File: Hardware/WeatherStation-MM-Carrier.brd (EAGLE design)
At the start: 67.3 x 58.4 mm, 154 parts, among them J11 microSD, J13 RJ11 - WIND, J15 MICROMOD-2222-C, J2 JTAG, J3 QWIIC_RIGHT_ANGLE, J7 RJ11 - RAIN, U1 BME280, U2 VEML6075, U3 AS3935, U5 AP7361C-33FGE

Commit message: Implementing some changes from design check list
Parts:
- removed U$24: (no value), buzzard_labels (3):STATION5
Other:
- board text added: "ROUTE OUT"
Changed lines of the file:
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@@
 <layer number="25" name="tNames" color="7" fill="1" visible="no" active="yes"/>
 <layer number="26" name="bNames" color="7" fill="1" visible="no" active="yes"/>
-<layer number="27" name="tValues" color="7" fill="1" visible="yes" active="yes"/>
+<layer number="27" name="tValues" color="7" fill="1" visible="no" active="yes"/>
 <layer number="28" name="bValues" color="7" fill="1" visible="no" active="yes"/>
 <layer number="29" name="tStop" color="7" fill="3" visible="no" active="yes"/>
@@
 <rectangle x1="20.32" y1="56.261" x2="25.4" y2="58.039" layer="21"/>
 <rectangle x1="20.32" y1="56.261" x2="25.4" y2="58.039" layer="22" rot="R180"/>
+<text x="36.83" y="40.64" size="0.254" layer="20" font="vector" ratio="15">ROUTE OUT</text>
+<text x="35.56" y="36.83" size="0.254" layer="20" font="vector" ratio="15" rot="R90">ROUTE OUT</text>
+<text x="40.64" y="39.37" size="0.254" layer="20" font="vector" ratio="15" rot="R270">ROUTE OUT</text>
 </plain>
 <attributes>
@@
 <element name="U$13" library="buzzard_labels (3)" package="SIG1" value="" x="66.04" y="37.211" smashed="yes" rot="R90"/>
 <element name="U$16" library="buzzard_labels (3)" package="WEATHER4" value="" x="17.907" y="37.338" smashed="yes"/>
-<element name="U$24" library="buzzard_labels (3)" package="STATION5" value="" x="18.542" y="35.306" smashed="yes"/>
 <element name="LOGO1" library="SparkFun-Aesthetics" package="SFE_LOGO_NAME_FLAME_.2" value="SFE_LOGO_NAME_FLAME.2_INCH" x="33.02" y="30.48" smashed="yes" rot="MR0"/>
 <element name="U$35" library="buzzard_labels (4)" package="MICROSD0" value="" x="4.826" y="48.26" smashed="yes"/>
@@
 <wire x1="43.4984" y1="41.7068" x2="43.4984" y2="44.1334" width="0.2032" layer="16"/>
 <via x="43.4984" y="41.7068" extent="1-16" drill="0.3048"/>
-<wire x1="29.1846" y1="39.751" x2="29.1846" y2="40.2336" width="0.2032" layer="1"/>
-<wire x1="29.1846" y1="40.2336" x2="30.2768" y2="41.3258" width="0.2032" layer="1"/>
-<wire x1="43.1174" y1="41.3258" x2="30.2768" y2="41.3258" width="0.2032" layer="1"/>
+<wire x1="31.5976" y1="41.3258" x2="43.1174" y2="41.3258" width="0.2032" layer="1"/>
 <wire x1="43.1174" y1="41.3258" x2="43.4984" y2="41.7068" width="0.2032" layer="1"/>
+<wire x1="29.1846" y1="39.751" x2="30.3276" y2="40.894" width="0.2032" layer="1"/>
+<wire x1="31.1658" y1="40.894" x2="31.5976" y2="41.3258" width="0.2032" layer="1"/>
+<wire x1="30.3276" y1="40.894" x2="31.1658" y2="40.894" width="0.2032" layer="1"/>
 </signal>
 <signal name="GND">

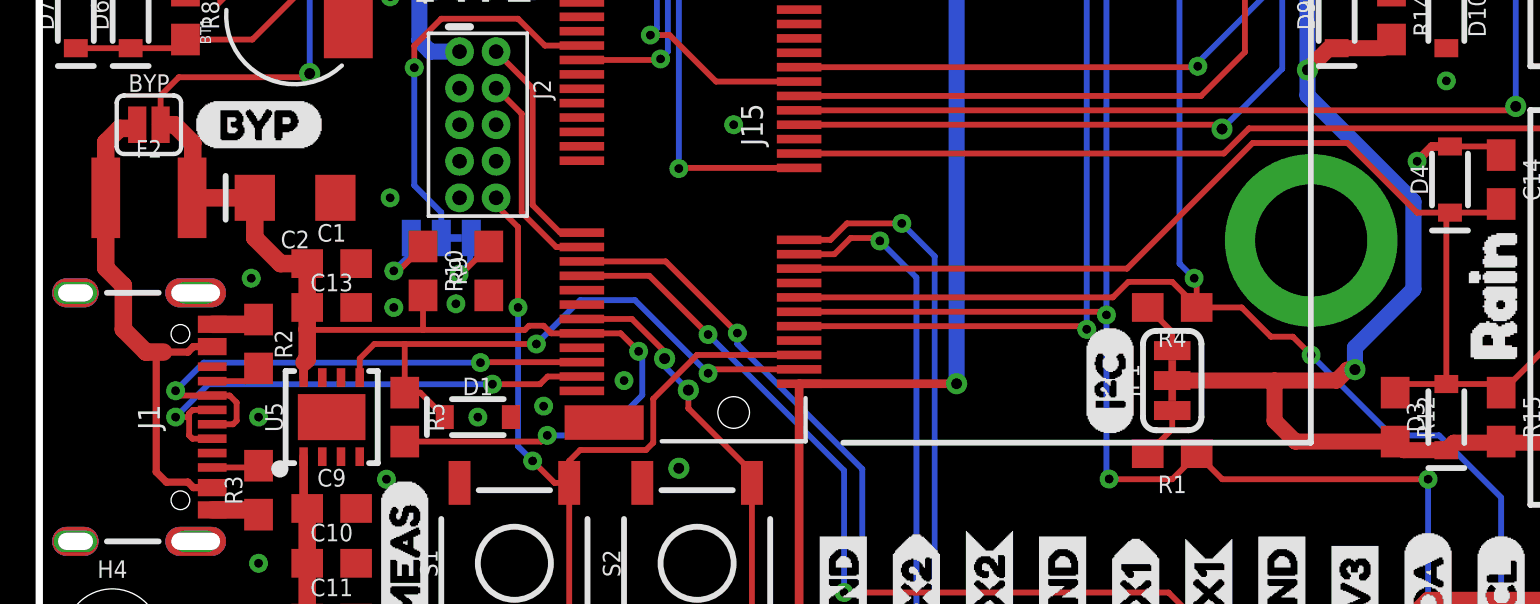
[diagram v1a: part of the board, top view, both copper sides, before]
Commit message: Added jumper on 3.3V_EN
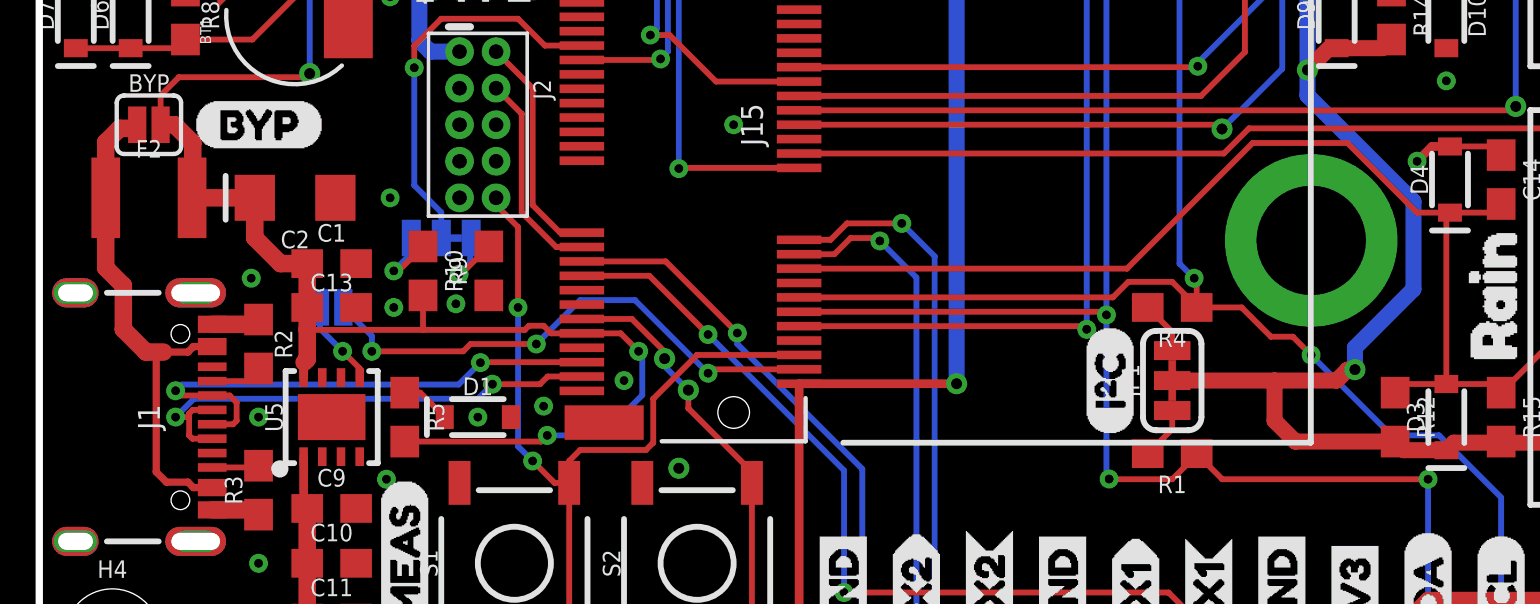
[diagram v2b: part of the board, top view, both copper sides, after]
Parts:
- removed U$63: (no value), buzzard_labels (3):STATION5
- added JP6: VE, SparkFun-Jumpers:SMT-JUMPER_2_NO_SILK
- added U$14: (no value), buzzard_labels (8):3#3V_EN0
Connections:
- net 3.3V_EN: now also JP6.1, JP6.2
- net SD_!CS!: now also J11.CS/DAT3; no longer J11.CS
- net SPI_MISO: now also J11.DO/DAT0; no longer J11.DO
- net SPI_MOSI: now also J11.DI/CMD; no longer J11.DI
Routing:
- net 3.3V_EN: track 21.3 -> 23.4 mm, vias 2 -> 4
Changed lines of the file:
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@@
 <element name="U$44" library="SparkFun-Aesthetics" package="SFE_LOGO_FLAME_.2" value="" x="24.384" y="43.815" smashed="yes"/>
 <element name="U$58" library="buzzard_labels (3)" package="WEATHER4" value="" x="38.862" y="24.13" smashed="yes" rot="MR0"/>
-<element name="U$63" library="buzzard_labels (3)" package="STATION5" value="" x="38.1" y="22.225" smashed="yes" rot="MR0"/>
 <element name="U$20" library="buzzard_labels (73)" package="ATMOSPHERIC0" value="" x="32.766" y="34.417" smashed="yes"/>
 <element name="U$64" library="buzzard_labels (73)" package="SENSOR1" value="" x="34.925" y="33.02" smashed="yes"/>
 <element name="U$67" library="SparkFun-MicroMod" package="MICROMOD_LOGO_.5" value="" x="23.622" y="39.624" smashed="yes"/>
 <element name="U$68" library="SparkFun-MicroMod" package="MICROMOD_LOGO_.5" value="" x="33.02" y="26.67" smashed="yes" rot="MR0"/>
+<element name="JP6" library="SparkFun-Jumpers" package="SMT-JUMPER_2_NO_SILK" package3d_urn="urn:adsk.eagle:package:39279/1" value="VE" x="10.16" y="13.97" smashed="yes" rot="MR0">
+<attribute name="NAME" x="10.16" y="15.113" size="0.6096" layer="26" font="vector" ratio="20" rot="MR0" align="bottom-center"/>
+<attribute name="VALUE" x="10.16" y="12.827" size="0.6096" layer="28" font="vector" ratio="20" rot="MR0" align="top-center"/>
+</element>
+<element name="U$14" library="buzzard_labels (8)" package="3#3V_EN0" value="" x="8.382" y="13.97" smashed="yes" rot="MR0"/>
 </elements>
 <signals>
@@
 <wire x1="4.9030875" y1="10.91" x2="4.7371" y2="11.0759875" width="0.2032" layer="1"/>
 <via x="4.7371" y="11.0759875" extent="1-16" drill="0.3048"/>
-<wire x1="4.7371" y1="11.0759875" x2="5.7134125" y2="12.0523" width="0.2032" layer="16"/>
-<wire x1="5.7134125" y1="12.0523" x2="15.3311375" y2="12.0523" width="0.2032" layer="16"/>
+<wire x1="4.7371" y1="11.0759875" x2="4.9514125" y2="11.2903" width="0.2032" layer="16"/>
+<wire x1="14.5691375" y1="11.2903" x2="15.3311375" y2="12.0523" width="0.2032" layer="16"/>
+<wire x1="14.5691375" y1="11.2903" x2="4.9514125" y2="11.2903" width="0.2032" layer="16"/>
 <via x="15.3311375" y="12.0523" extent="1-16" drill="0.3048"/>
 <wire x1="15.3488375" y1="12.07" x2="15.3311375" y2="12.0523" width="0.2032" layer="1"/>
@@
 <wire x1="5.207" y1="10.16" x2="4.7371" y2="10.16" width="0.2032" layer="1"/>
 <via x="4.7371" y="10.16" extent="1-16" drill="0.3048"/>
-<wire x1="4.7371" y1="10.16" x2="5.8801" y2="11.303" width="0.2032" layer="16"/>
-<wire x1="5.8801" y1="11.303" x2="15.748" y2="11.303" width="0.2032" layer="16"/>
+<wire x1="4.7371" y1="10.16" x2="5.3721" y2="10.795" width="0.2032" layer="16"/>
+<wire x1="15.24" y1="10.795" x2="15.748" y2="11.303" width="0.2032" layer="16"/>
+<wire x1="15.24" y1="10.795" x2="5.3721" y2="10.795" width="0.2032" layer="16"/>
 <via x="15.748" y="11.303" extent="1-16" drill="0.3048"/>
 <wire x1="15.748" y1="11.303" x2="17.399" y2="11.303" width="0.2032" layer="1"/>
@@
 <contactref element="J5" pad="2"/>
 <contactref element="U3" pad="13"/>
-<contactref element="J11" pad="DI"/>
+<contactref element="J11" pad="DI/CMD"/>
 <wire x1="45.593" y1="46.0216" x2="45.0874" y2="46.0216" width="0.2032" layer="1"/>
 <wire x1="14.478" y1="40.25" x2="5.81" y2="40.25" width="0.2032" layer="1"/>
@@
 <contactref element="J5" pad="3"/>
 <contactref element="U3" pad="12"/>
-<contactref element="J11" pad="DO"/>
+<contactref element="J11" pad="DO/DAT0"/>
 <via x="27.92650625" y="27.31849375" extent="1-16" drill="0.381"/>
 <contactref element="J15" pad="64"/>
@@
 </signal>
 <signal name="SD_!CS!">
-<contactref element="J11" pad="CS"/>
+<contactref element="J11" pad="CS/DAT3"/>
 <wire x1="6.21" y1="39.15" x2="13.428" y2="39.15" width="0.2032" layer="1"/>
 <wire x1="15.113" y1="37.465" x2="13.428" y2="39.15" width="0.2032" layer="1"/>
@@
 <wire x1="12.7" y1="11.01" x2="13.24" y2="11.01" width="0.2032" layer="1"/>
 <wire x1="13.24" y1="11.01" x2="14.09" y2="10.16" width="0.2032" layer="1"/>
-<wire x1="11.643" y1="12.7" x2="12.7" y2="12.7" width="0.2032" layer="1"/>
-<wire x1="12.7" y1="12.7" x2="12.7" y2="11.01" width="0.2032" layer="1"/>
-<wire x1="12.7" y1="12.7" x2="17.272" y2="12.7" width="0.2032" layer="1"/>
 <via x="17.272" y="12.7" extent="1-16" drill="0.3048"/>
 <wire x1="17.272" y1="12.7" x2="18.796" y2="14.224" width="0.2032" layer="16"/>
@@
 <wire x1="23.241" y1="11.684" x2="20.701" y2="14.224" width="0.2032" layer="16"/>
 <wire x1="23.377" y1="11.82" x2="23.241" y2="11.684" width="0.2032" layer="1"/>
-<wire x1="11.135" y1="11.535" x2="11.135" y2="12.192" width="0.2032" layer="1"/>
-<wire x1="11.135" y1="12.192" x2="11.643" y2="12.7" width="0.2032" layer="1"/>
 <contactref element="J15" pad="4"/>
 <wire x1="26.405" y1="11.82" x2="23.377" y2="11.82" width="0.2032" layer="1"/>
+<contactref element="JP6" pad="2"/>
+<contactref element="JP6" pad="1"/>
+<wire x1="11.135" y1="11.535" x2="11.135" y2="11.852" width="0.2032" layer="1"/>
+<wire x1="11.135" y1="11.852" x2="10.541" y2="12.446" width="0.2032" layer="1"/>
+<via x="10.541" y="12.446" extent="1-16" drill="0.3048"/>
+<wire x1="10.541" y1="12.446" x2="9.7536" y2="13.2334" width="0.2032" layer="16"/>
+<wire x1="9.7536" y1="13.2334" x2="9.7536" y2="13.97" width="0.2032" layer="16"/>
+<wire x1="10.5664" y1="13.97" x2="11.557" y2="12.9794" width="0.2032" layer="16"/>
+<via x="11.557" y="12.446" extent="1-16" drill="0.3048"/>
+<wire x1="11.557" y1="12.446" x2="14.732" y2="12.446" width="0.2032" layer="1"/>
+<wire x1="14.986" y1="12.7" x2="14.732" y2="12.446" width="0.2032" layer="1"/>
+<wire x1="14.986" y1="12.7" x2="17.272" y2="12.7" width="0.2032" layer="1"/>
+<wire x1="11.557" y1="12.9794" x2="11.557" y2="12.446" width="0.2032" layer="16"/>
+<wire x1="11.135" y1="11.535" x2="12.7" y2="11.01" width="0" layer="19" extent="1-1"/>
+<wire x1="10.5664" y1="13.97" x2="9.7536" y2="13.97" width="0" layer="19" extent="16-16"/>
 </signal>
 <signal name="N$4">

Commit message: Update weather meter circuitry
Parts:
- removed R12, R13: 10k, SparkFun-Resistors:0603
- R15, R16: value 100k -> 43k
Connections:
- net 3.3V: no longer R12.2, R13.2
- net RAIN: no longer R12.1
- net WSPEED: no longer R13.1
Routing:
- net RAIN: track 40.8 -> 38.9 mm
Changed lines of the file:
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@@
 <attribute name="VALUE" x="10.16" y="2.413" size="0.6096" layer="27" font="vector" ratio="20" align="top-center"/>
-</element>
-<element name="R12" library="SparkFun-Resistors" package="0603" value="10k" x="47.117" y="10.16" smashed="yes" rot="R270">
-<attribute name="NAME" x="47.879" y="10.16" size="0.6096" layer="25" font="vector" ratio="20" rot="R270" align="bottom-center"/>
-<attribute name="PROD_ID" value="RES-00824" x="47.117" y="10.16" size="1.778" layer="27" font="vector" ratio="15" rot="R270" display="off"/>
-<attribute name="VALUE" x="46.355" y="10.16" size="0.6096" layer="27" font="vector" ratio="20" rot="R270" align="top-center"/>
-</element>
-<element name="R13" library="SparkFun-Resistors" package="0603" value="10k" x="44.45" y="29.21" smashed="yes" rot="R270">
-<attribute name="NAME" x="45.212" y="29.21" size="0.6096" layer="25" font="vector" ratio="20" rot="R270" align="bottom-center"/>
-<attribute name="PROD_ID" value="RES-00824" x="44.45" y="29.21" size="1.778" layer="27" font="vector" ratio="15" rot="R270" display="off"/>
-<attribute name="VALUE" x="43.688" y="29.21" size="0.6096" layer="27" font="vector" ratio="20" rot="R270" align="top-center"/>
 </element>
 <element name="R14" library="SparkFun-Resistors" package="0603" value="10k" x="46.99" y="24.13" smashed="yes" rot="R270">
@@
 <attribute name="VALUE" x="48.133" y="24.13" size="0.6096" layer="27" font="vector" ratio="20" rot="R270" align="top-center"/>
 </element>
-<element name="R15" library="SparkFun-Resistors" package="0603" value="100k" x="50.8" y="10.16" smashed="yes" rot="R270">
+<element name="R15" library="SparkFun-Resistors" package="0603" value="43k" x="50.8" y="10.16" smashed="yes" rot="R270">
 <attribute name="NAME" x="51.562" y="10.16" size="0.6096" layer="25" font="vector" ratio="20" rot="R270" align="bottom-center"/>
-<attribute name="PROD_ID" value="RES-07828" x="50.8" y="10.16" size="1.778" layer="27" font="vector" ratio="15" rot="R270" display="off"/>
-<attribute name="VALUE" x="50.038" y="10.16" size="0.6096" layer="27" font="vector" ratio="20" rot="R270" align="top-center"/>
-</element>
-<element name="R16" library="SparkFun-Resistors" package="0603" value="100k" x="48.26" y="29.21" smashed="yes" rot="R270">
+<attribute name="PROD_ID" value="RES-07858" x="50.8" y="10.16" size="1.778" layer="27" font="vector" ratio="15" rot="R270" display="off"/>
+<attribute name="VALUE" value="43k" x="50.038" y="10.16" size="0.6096" layer="27" font="vector" ratio="20" rot="R270" align="top-center"/>
+</element>
+<element name="R16" library="SparkFun-Resistors" package="0603" value="43k" x="48.26" y="29.21" smashed="yes" rot="R270">
 <attribute name="NAME" x="49.022" y="29.21" size="0.6096" layer="25" font="vector" ratio="20" rot="R270" align="bottom-center"/>
-<attribute name="PROD_ID" value="RES-07828" x="48.26" y="29.21" size="1.778" layer="27" font="vector" ratio="15" rot="R270" display="off"/>
-<attribute name="VALUE" x="47.498" y="29.21" size="0.6096" layer="27" font="vector" ratio="20" rot="R270" align="top-center"/>
+<attribute name="PROD_ID" value="RES-07858" x="48.26" y="29.21" size="1.778" layer="27" font="vector" ratio="15" rot="R270" display="off"/>
+<attribute name="VALUE" value="43k" x="47.498" y="29.21" size="0.6096" layer="27" font="vector" ratio="20" rot="R270" align="top-center"/>
 </element>
 <element name="C12" library="SparkFun-Capacitors" package="0603" value="0.1uF" x="48.26" y="33.02" smashed="yes" rot="R270">
@@
 <contactref element="R7" pad="2"/>
 <contactref element="R21" pad="2"/>
-<contactref element="R12" pad="2"/>
-<contactref element="R13" pad="2"/>
 <contactref element="R14" pad="2"/>
 <contactref element="D3" pad="C"/>
@@
 <wire x1="45.466" y1="11.811" x2="45.085" y2="11.43" width="0.5588" layer="1"/>
 <wire x1="45.72" y1="11.811" x2="45.466" y2="11.811" width="0.5588" layer="1"/>
-<wire x1="48.895" y1="9.01" x2="47.417" y2="9.01" width="0.5588" layer="1"/>
-<wire x1="47.417" y1="9.01" x2="47.117" y2="9.31" width="0.5588" layer="1"/>
 <wire x1="54.737" y1="9.271" x2="56.65" y2="7.358" width="0.5588" layer="1"/>
 <wire x1="45.085" y1="22.98" x2="46.69" y2="22.98" width="0.5588" layer="1"/>
 <wire x1="46.69" y1="22.98" x2="46.99" y2="23.28" width="0.2032" layer="1"/>
-<wire x1="44.45" y1="28.36" x2="46.055" y2="28.36" width="0.5588" layer="1"/>
-<wire x1="46.055" y1="28.36" x2="46.355" y2="28.06" width="0.5588" layer="1"/>
 <wire x1="46.355" y1="28.06" x2="47.96" y2="28.06" width="0.5588" layer="1"/>
 <wire x1="47.96" y1="28.06" x2="48.26" y2="28.36" width="0.2032" layer="1"/>
@@
 <wire x1="54.737" y1="9.271" x2="50.839" y2="9.271" width="0.5588" layer="1"/>
 <wire x1="50.839" y1="9.271" x2="50.8" y2="9.31" width="0.5588" layer="1"/>
-<wire x1="47.117" y1="9.31" x2="43.649" y2="9.31" width="0.5588" layer="1"/>
 <wire x1="42.926" y1="10.033" x2="42.926" y2="11.43" width="0.5588" layer="1"/>
-<wire x1="43.649" y1="9.31" x2="42.926" y2="10.033" width="0.5588" layer="1"/>
 <wire x1="48.895" y1="9.01" x2="49.156" y2="9.271" width="0.5588" layer="1"/>
 <wire x1="49.156" y1="9.271" x2="50.839" y2="9.271" width="0.5588" layer="1"/>
@@
 <via x="43.1927" y="31.75" extent="1-16" drill="0.381"/>
 <wire x1="43.1927" y1="31.75" x2="43.18" y2="31.7373" width="0.5588" layer="16"/>
-<wire x1="44.45" y1="28.36" x2="43.2807" y2="28.36" width="0.5588" layer="1"/>
-<wire x1="43.2807" y1="28.36" x2="43.1927" y2="28.448" width="0.5588" layer="1"/>
 <via x="43.1927" y="28.448" extent="1-16" drill="0.381"/>
 <wire x1="44.069" y1="22.225" x2="44.069" y2="26.416" width="0.5588" layer="16"/>
@@
 <wire x1="31.877" y1="11.32" x2="31.877" y2="11.303" width="0.5588" layer="16"/>
 <via x="31.877" y="11.32" extent="1-16" drill="0.381"/>
+<wire x1="46.355" y1="28.06" x2="43.5807" y2="28.06" width="0.5588" layer="1"/>
+<wire x1="43.5807" y1="28.06" x2="43.1927" y2="28.448" width="0.5588" layer="1"/>
+<wire x1="48.895" y1="9.01" x2="43.949" y2="9.01" width="0.5588" layer="1"/>
+<wire x1="43.949" y1="9.01" x2="42.926" y2="10.033" width="0.5588" layer="1"/>
 </signal>
 <signal name="USB_D-">
@@
 <signal name="RAIN">
 <contactref element="J7" pad="3"/>
-<contactref element="R12" pad="1"/>
 <contactref element="D3" pad="A"/>
 <contactref element="D4" pad="C"/>
@@
 <wire x1="48.895" y1="11.31" x2="50.5" y2="11.31" width="0.2032" layer="1"/>
 <wire x1="50.8" y1="11.01" x2="50.5" y2="11.31" width="0.2032" layer="1"/>
-<wire x1="48.895" y1="11.31" x2="47.417" y2="11.31" width="0.2032" layer="1"/>
-<wire x1="47.417" y1="11.31" x2="47.117" y2="11.01" width="0.2032" layer="1"/>
 <wire x1="50.8" y1="17.565" x2="50.5" y2="17.265" width="0.2032" layer="1"/>
 <wire x1="50.5" y1="17.265" x2="49.022" y2="17.265" width="0.2032" layer="1"/>
@@
 <signal name="WSPEED">
 <contactref element="J13" pad="3"/>
-<contactref element="R13" pad="1"/>
 <contactref element="D8" pad="C"/>
 <contactref element="D5" pad="A"/>
@@
 <wire x1="46.355" y1="30.36" x2="47.96" y2="30.36" width="0.2032" layer="1"/>
 <wire x1="47.96" y1="30.36" x2="48.26" y2="30.06" width="0.2032" layer="1"/>
-<wire x1="46.355" y1="30.36" x2="46.355" y2="30.099" width="0.2032" layer="1"/>
-<wire x1="44.489" y1="30.099" x2="44.45" y2="30.06" width="0.2032" layer="1"/>
+<wire x1="46.355" y1="30.36" x2="46.355" y2="30.353" width="0.2032" layer="1"/>
 <wire x1="48.26" y1="32.17" x2="47.96" y2="31.87" width="0.2032" layer="1"/>
 <wire x1="47.96" y1="31.87" x2="46.355" y2="31.87" width="0.2032" layer="1"/>
@@
 <wire x1="36.3986" y1="30.0486" x2="36.449" y2="30.099" width="0.2032" layer="16"/>
 <via x="36.449" y="30.099" extent="1-16" drill="0.3048"/>
-<wire x1="36.449" y1="30.099" x2="44.489" y2="30.099" width="0.2032" layer="1"/>
-<wire x1="44.489" y1="30.099" x2="46.355" y2="30.099" width="0.2032" layer="1"/>
+<wire x1="36.449" y1="30.099" x2="36.703" y2="30.353" width="0.2032" layer="1"/>
+<wire x1="46.355" y1="30.353" x2="36.703" y2="30.353" width="0.2032" layer="1"/>
 </signal>
 <signal name="N$15">
